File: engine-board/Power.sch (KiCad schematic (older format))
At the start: 10 parts, among them J401 USB/SER/CHRGR, J402 Power Rail, J403 INA219 Engine Current Sensor, J404 Switch Bulkhead, J405 Battery Input, J406 3V Current Sensor, J407 5V Current Sensor, U401 Pololu_2812, U402 R-78B3.3-2.0, U403 R-78B5.0-2.0

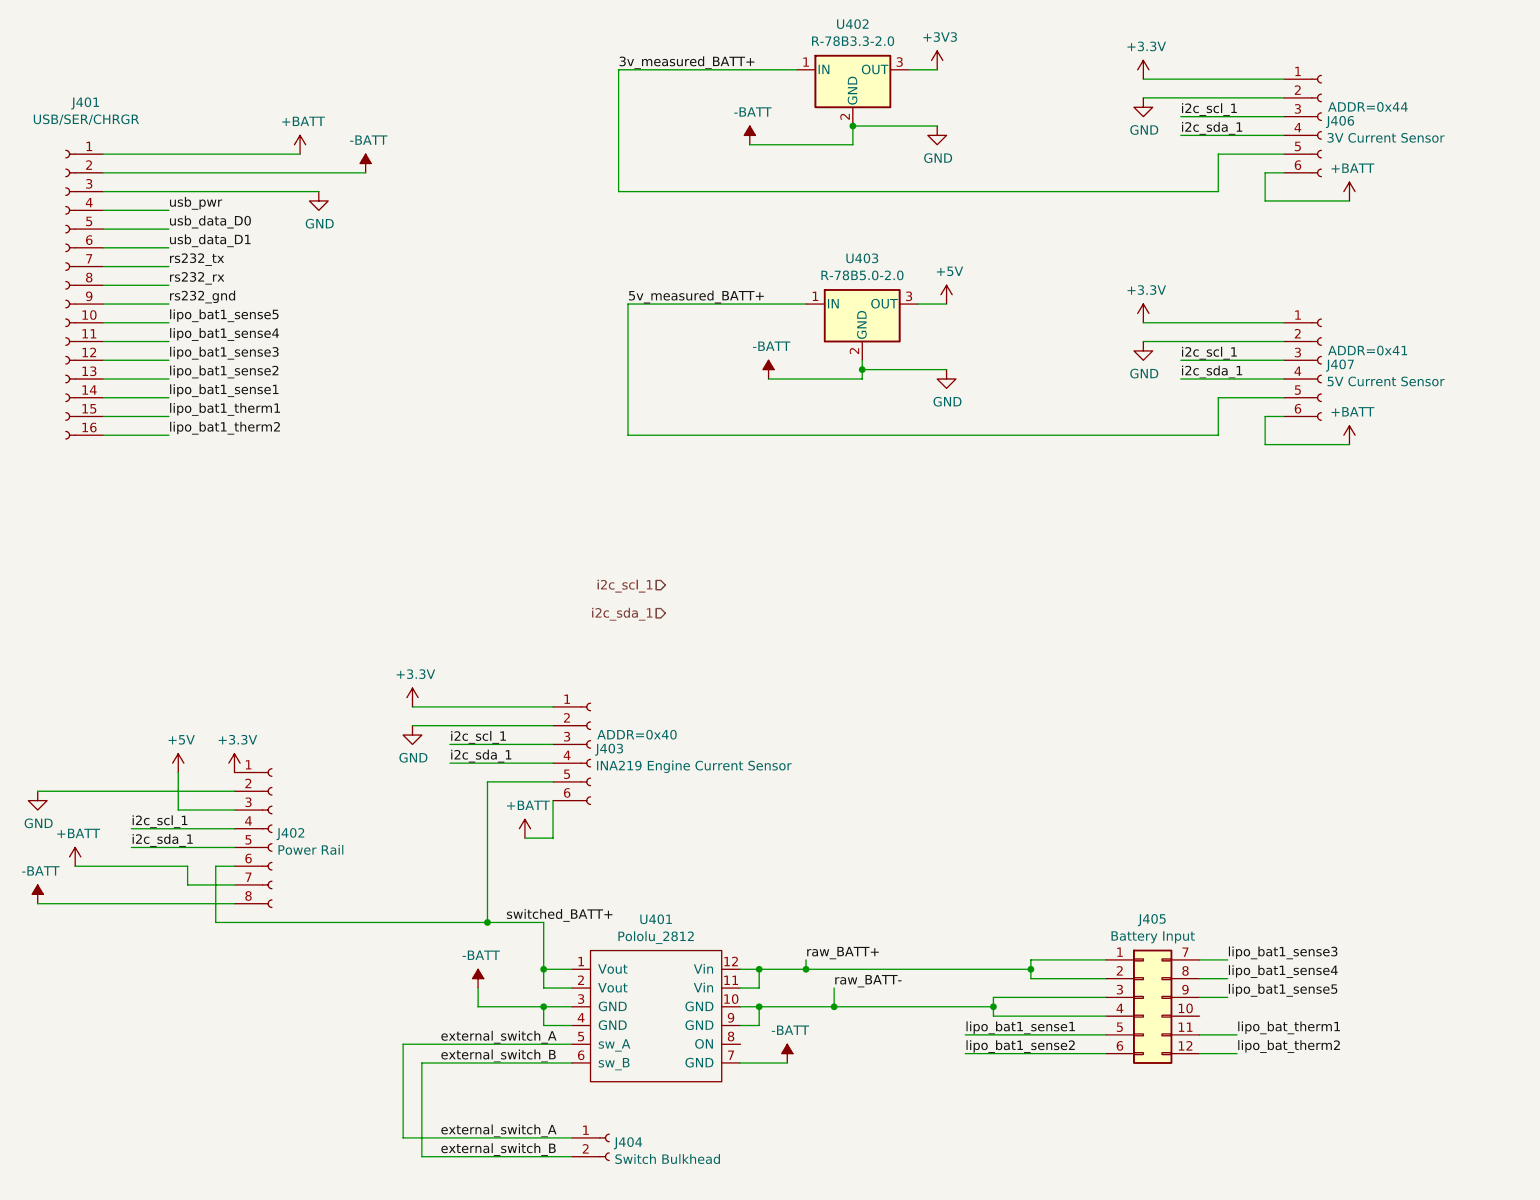
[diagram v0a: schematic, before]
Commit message: pcb parts done, footprints updated, ready for routing
pre-routing step..
- finalized footprints
- verified layout, size, mounting holes (1.75" apart)
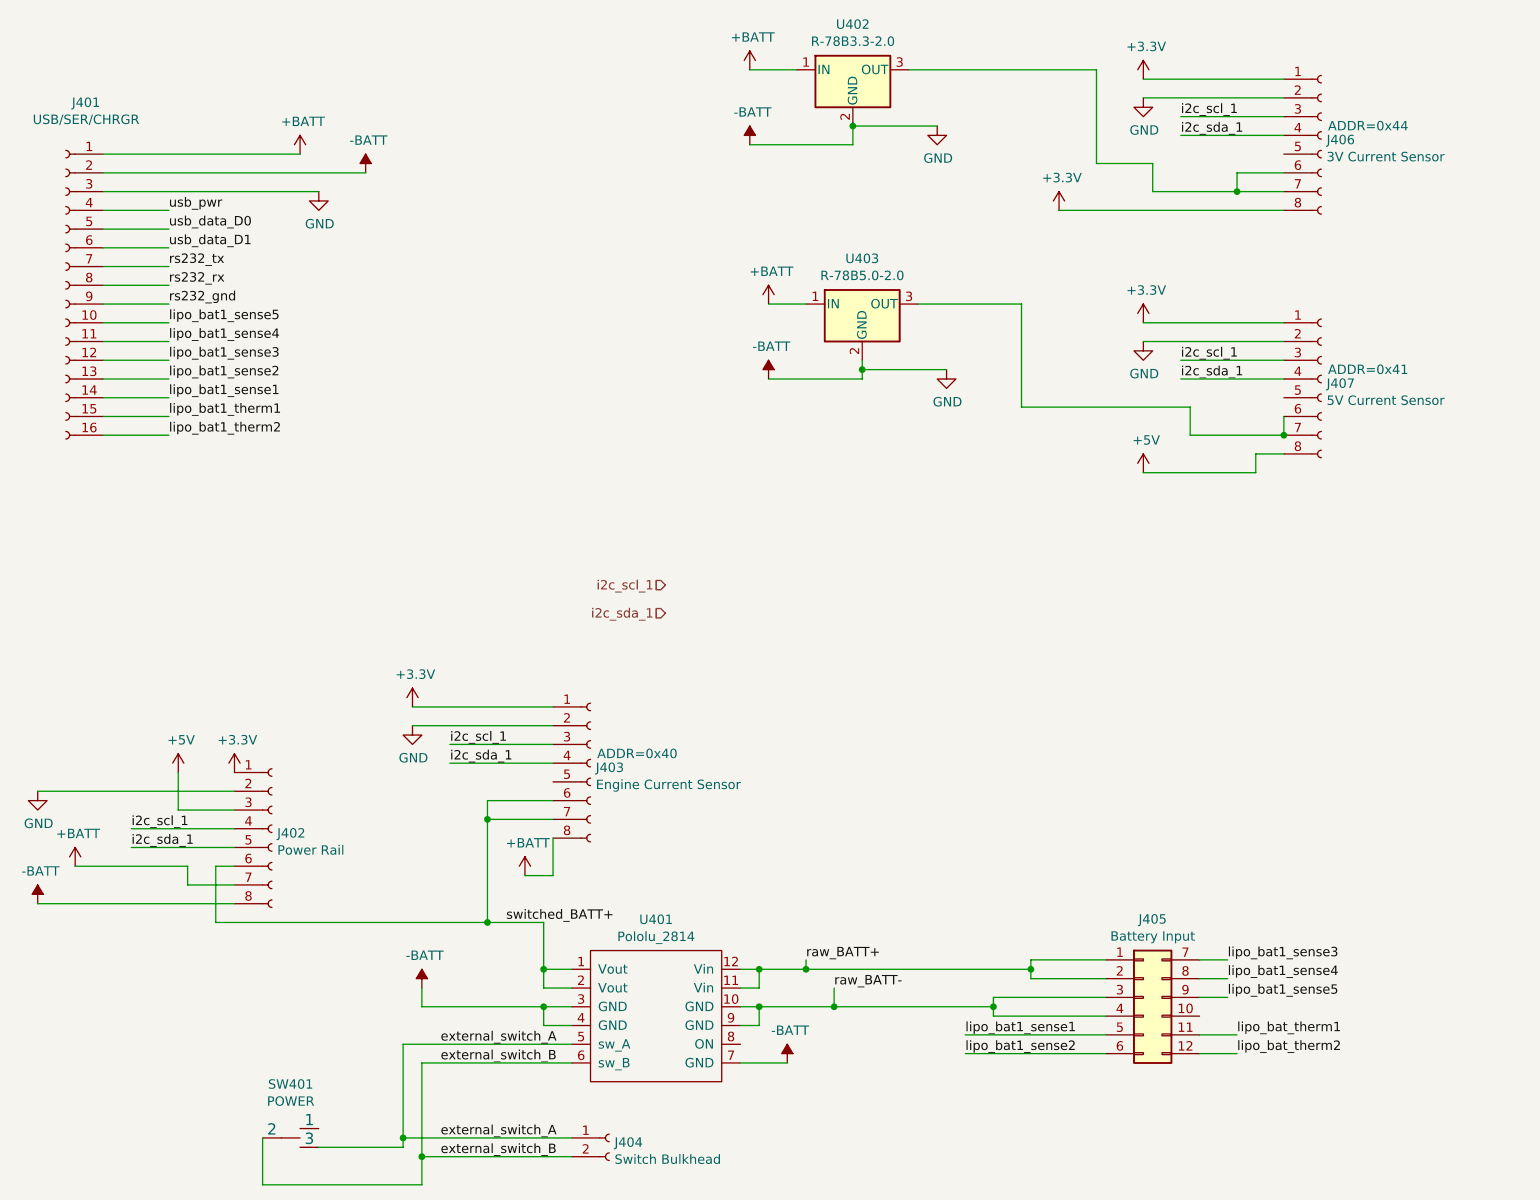
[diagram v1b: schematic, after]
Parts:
- removed J403: INA219 Engine Current Sensor, Connector_PinSocket_2.54mm:PinSocket_1x06_P2.54mm_Vertical, symbol Connector:Conn_01x06_Female
- removed J406: 3V Current Sensor, Connector_PinSocket_2.54mm:PinSocket_1x06_P2.54mm_Vertical, symbol Connector:Conn_01x06_Female
- removed J407: 5V Current Sensor, Connector_PinSocket_2.54mm:PinSocket_1x06_P2.54mm_Vertical, symbol Connector:Conn_01x06_Female
- added J403: Engine Current Sensor, Connector_PinSocket_2.54mm:PinSocket_1x08_P2.54mm_Vertical, symbol Connector:Conn_01x08_Female
- added J406: 3V Current Sensor, Connector_PinSocket_2.54mm:PinSocket_1x08_P2.54mm_Vertical, symbol Connector:Conn_01x08_Female
- added J407: 5V Current Sensor, Connector_PinSocket_2.54mm:PinSocket_1x08_P2.54mm_Vertical, symbol Connector:Conn_01x08_Female
- added SW401: POWER, Module:SliderSwitch_Simple, symbol MiscellaneousDevices:SWITCH_SPDT
- U401: value Pololu_2812 -> Pololu_2814; footprint Module:Pololu_SlidePwrSwitch -> Module:Pololu_Breakout-16_15.2x20.3mm; Link https://www.pololu.com/product/2812 -> https://www.pololu.com/product/2814; MPM 2812 -> 2814
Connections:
- net 3v_measured_BATT+ is gone; now on net +BATT: U402.1 (IN)
- net 5v_measured_BATT+ is gone; now on net +BATT: U403.1 (IN)
- net +3V3: now also J403.1 (Pin_1), J406.1 (Pin_1), J406.8 (Pin_8), J407.1 (Pin_1); no longer U402.3 (OUT)
- net +5V: now also J407.8 (Pin_8); no longer U403.3 (OUT)
- net +BATT: now also J403.8 (Pin_8)
- net -BATT: now also J403.2 (Pin_2), J406.2 (Pin_2), J407.2 (Pin_2)
- net external_switch_A: now also SW401.3
- net external_switch_B: now also SW401.2
- net i2c_scl_1: now also J403.3 (Pin_3), J406.3 (Pin_3), J407.3 (Pin_3)
- net i2c_sda_1: now also J403.4 (Pin_4), J406.4 (Pin_4), J407.4 (Pin_4)
- net switched_BATT+: now also J403.6 (Pin_6), J403.7 (Pin_7)
- new net: J406.6 (Pin_6), J406.7 (Pin_7), U402.3 (OUT)
- new net: J407.6 (Pin_6), J407.7 (Pin_7), U403.3 (OUT)

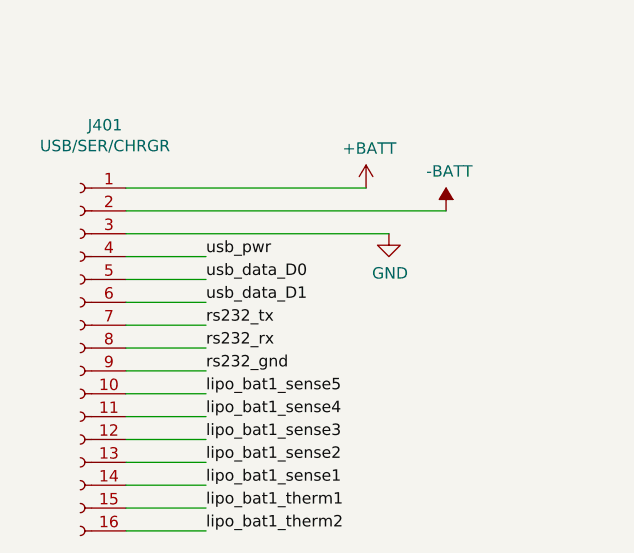
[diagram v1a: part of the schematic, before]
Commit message: shortend pcb, ready to route
ready to route, shortend pcb, layout complete
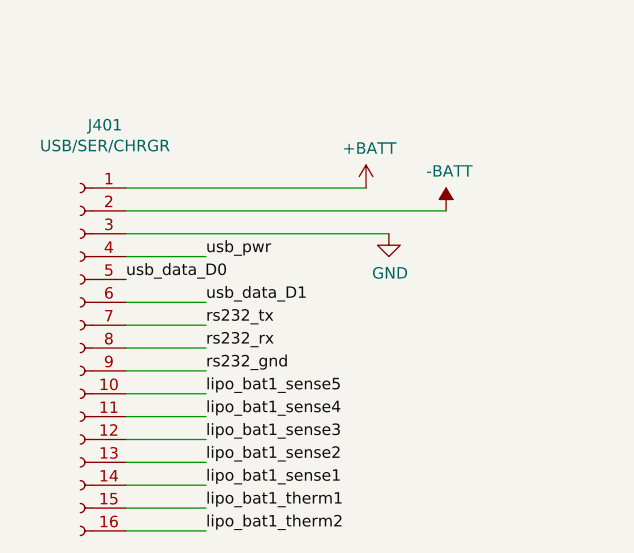
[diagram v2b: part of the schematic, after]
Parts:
- J401: footprint Connector_Molex:Molex_Micro-Fit_3.0_43045-1600_2x08_P3.00mm_Horizontal -> Connector_Molex:Molex_Micro-Fit_3.0_43045-1621_2x08-1MP_P3.00mm_Horizontal; Link https://www.digikey.com/en/products/detail/molex/0430451202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 -> https://www.digikey.com/en/products/detail/molex/0430451623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; MPN 0430451202 -> 430451623; Price 4.98 -> 6.91
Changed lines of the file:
@@
 F 0 "J401" H 1142 3025 50  0000 C CNN
 F 1 "USB/SER/CHRGR" H 1142 2934 50  0000 C CNN
-F 2 "Connector_Molex:Molex_Micro-Fit_3.0_43045-1600_2x08_P3.00mm_Horizontal" H 1142 2843 50  0001 C CNN
+F 2 "Connector_Molex:Molex_Micro-Fit_3.0_43045-1621_2x08-1MP_P3.00mm_Horizontal" H 1142 2843 50  0001 C CNN
 F 3 "~" H 1250 2050 50  0001 C CNN
-F 4 "https://www.digikey.com/en/products/detail/molex/0430451202/252537" H 1250 2050 50  0001 C CNN "Link"
+F 4 "https://www.digikey.com/en/products/detail/molex/0430451623/3044583?s=N4IgTCBcDaICwGYAMcCsBGAbGBIC6AvkA" H 1250 2050 50  0001 C CNN "Link"
 F 5 "Molex" H 1250 2050 50  0001 C CNN "MANUFACTURER"
-F 6 "0430451202" H 1250 2050 50  0001 C CNN "MPN"
-F 7 "4.98" H 1250 2050 50  0001 C CNN "Price"
+F 6 "430451623" H 1250 2050 50  0001 C CNN "MPN"
+F 7 "6.91" H 1250 2050 50  0001 C CNN "Price"
 	1    1250 2050
 	-1   0    0    -1
@@
 Text Label 1800 1650 0    50   ~ 0
 usb_pwr
-Text Label 1800 1750 0    50   ~ 0
+Text Label 1450 1750 0    50   ~ 0
 usb_data_D0
 Text Label 1800 1850 0    50   ~ 0
@@
 	1450 1650 1800 1650
 Wire Wire Line
-	1450 1750 1800 1750
-Wire Wire Line
 	1450 1850 1800 1850

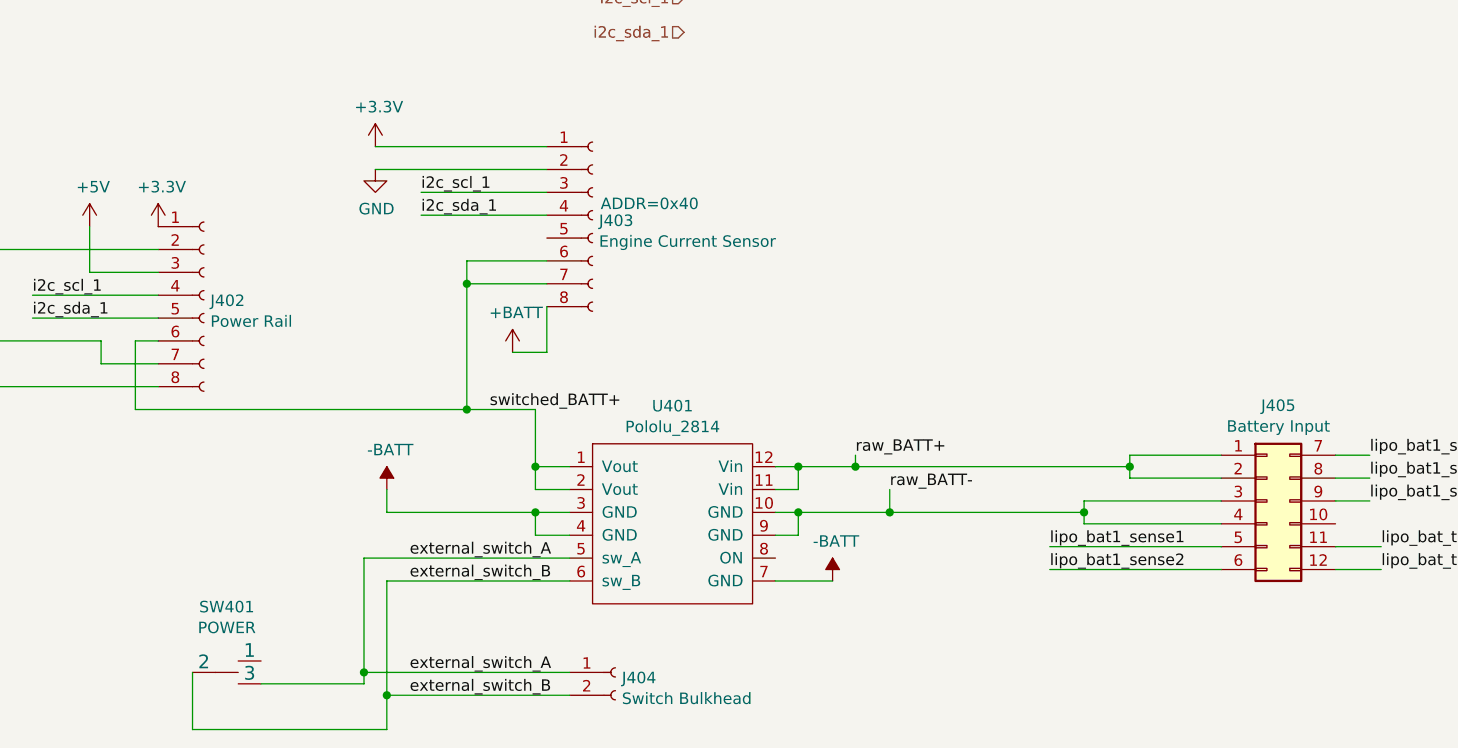
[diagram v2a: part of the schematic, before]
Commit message: ready for layout
- added batt solder tabs
- swapped some terminal blocks with microfit connectors
- shortened board, tightened layout
- tried to space everything out properly
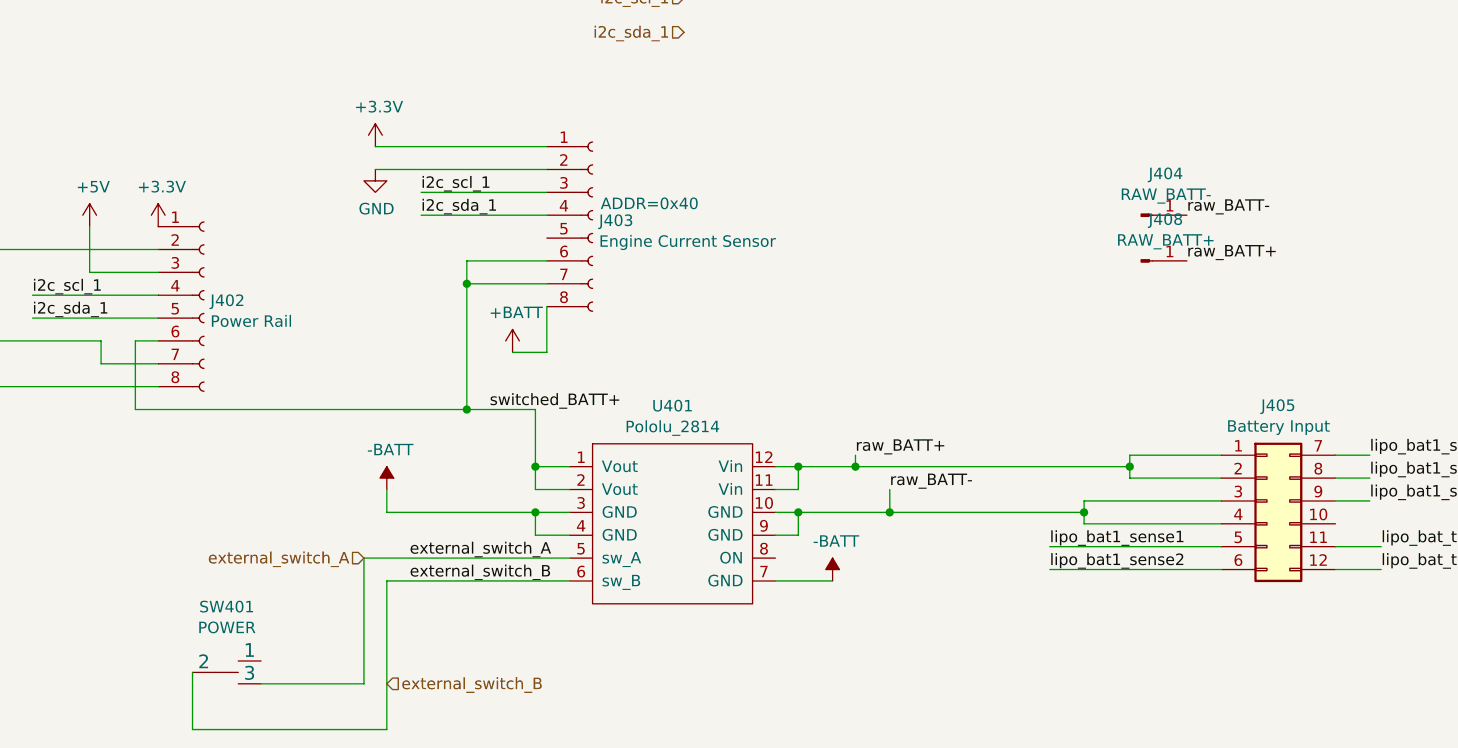
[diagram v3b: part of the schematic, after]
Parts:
- removed J404: Switch Bulkhead, TerminalBlock_CUI:CUI_TBP01R1W-508-02BE, symbol Connector:Conn_01x02_Female
- added J404: RAW_BATT-, TestPoint:TestPoint_Pad_4.0x4.0mm, symbol Connector:Conn_01x01_Male
- added J408: RAW_BATT+, TestPoint:TestPoint_Pad_4.0x4.0mm, symbol Connector:Conn_01x01_Male
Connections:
- net raw_BATT+: now also J408.1 (Pin_1)
- net raw_BATT-: now also J404.1 (Pin_1)
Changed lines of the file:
@@
 	1    0    0    -1
 $EndComp
-$Comp
-L Connector:Conn_01x02_Female J?
-U 1 1 61BB0ACA
-P 4150 6600
-AR Path="/61BB0ACA" Ref="J?"  Part="1"
-AR Path="/61B60659/61BB0ACA" Ref="J404"  Part="1"
-F 0 "J404" H 4178 6576 50  0000 L CNN
-F 1 "Switch Bulkhead" H 4178 6485 50  0000 L CNN
-F 2 "TerminalBlock_CUI:CUI_TBP01R1W-508-02BE" H 4150 6600 50  0001 C CNN
-F 3 "~" H 4150 6600 50  0001 C CNN
-F 4 "https://www.digikey.com/en/products/detail/cui-devices/TBP01R1W-508-02BE/10238425" H 4150 6600 50  0001 C CNN "Link"
-F 5 "CUI Devices" H 4150 6600 50  0001 C CNN "MANUFACTURER"
-F 6 "TBP01R1W-508-02BE" H 4150 6600 50  0001 C CNN "MPN"
-F 7 "0.77" H 4150 6600 50  0001 C CNN "Price"
-	1    4150 6600
-	1    0    0    -1
-$EndComp
-Text Label 3250 6600 0    50   ~ 0
-external_switch_A
-Text Label 3250 6700 0    50   ~ 0
-external_switch_B
 Wire Wire Line
 	4850 6200 5100 6200
@@
 	6400 5700 6400 5750
 Wire Wire Line
-	3050 6100 3050 6600
-Wire Wire Line
-	3050 6600 3950 6600
-Wire Wire Line
 	3050 6100 3950 6100
-Wire Wire Line
-	3150 6200 3150 6700
-Wire Wire Line
-	3150 6700 3950 6700
 Wire Wire Line
 	3150 6200 3950 6200
@@
 	2300 6850 3150 6850
 Wire Wire Line
-	3150 6850 3150 6700
-Connection ~ 3150 6700
-Wire Wire Line
 	2600 6650 3050 6650
-Wire Wire Line
-	3050 6650 3050 6600
-Connection ~ 3050 6600
+Text HLabel 3050 6100 0    50   Input ~ 0
+external_switch_A
+Text HLabel 3150 6650 2    50   Input ~ 0
+external_switch_B
+Wire Wire Line
+	3050 6100 3050 6650
+Wire Wire Line
+	3150 6200 3150 6850
+$Comp
+L Connector:Conn_01x01_Male J404
+U 1 1 6201AA81
+P 6450 4600
+F 0 "J404" H 6558 4781 50  0000 C CNN
+F 1 "RAW_BATT-" H 6558 4690 50  0000 C CNN
+F 2 "TestPoint:TestPoint_Pad_4.0x4.0mm" H 6450 4600 50  0001 C CNN
+F 3 "~" H 6450 4600 50  0001 C CNN
+	1    6450 4600
+	1    0    0    -1
+$EndComp
+$Comp
+L Connector:Conn_01x01_Male J408
+U 1 1 6201B167
+P 6450 4800
+F 0 "J408" H 6558 4981 50  0000 C CNN
+F 1 "RAW_BATT+" H 6558 4890 50  0000 C CNN
+F 2 "TestPoint:TestPoint_Pad_4.0x4.0mm" H 6450 4800 50  0001 C CNN
+F 3 "~" H 6450 4800 50  0001 C CNN
+	1    6450 4800
+	1    0    0    -1
+$EndComp
+Text Label 6650 4800 0    50   ~ 0
+raw_BATT+
+Text Label 6650 4600 0    50   ~ 0
+raw_BATT-
 $EndSCHEMATC
